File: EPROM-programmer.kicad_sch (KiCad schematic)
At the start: 2 parts, among them U1 ATmega1284-P, U2 MCP2221AxP

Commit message: Some initial stuff
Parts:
- added C1, C2: 22p, Capacitor_THT:C_Rect_L4.6mm_W3.0mm_P2.50mm_MKS02_FKP02, symbol Device:C
- added C3: 100n, Capacitor_THT:C_Rect_L4.6mm_W3.0mm_P2.50mm_MKS02_FKP02, symbol Device:C
- added J1: Conn_02x12_Counter_Clockwise, Local:DIP_Socket-24_W11.9_W12.7_W15.24_W17.78_W18.5_3M_224-1275-00-0602J, symbol Connector_Generic:Conn_02x12_Counter_Clockwise
- added P1: USB_C_Plug_USB2.0, Connector_USB:USB_C_Receptacle_GCT_USB4085, symbol Connector:USB_C_Receptacle_USB2.0
- added R1, R2, R3: 5K1, Resistor_THT:R_Axial_DIN0207_L6.3mm_D2.5mm_P10.16mm_Horizontal, symbol Device:R
- added R4, R5: 470, Resistor_THT:R_Axial_DIN0207_L6.3mm_D2.5mm_P10.16mm_Horizontal, symbol Device:R
- added SW1: SW_Push, symbol Switch:SW_Push
- added Y1: 20M, Crystal:Crystal_HC49-U_Vertical, symbol Device:Crystal
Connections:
- net +5V: now reaches U2.1 (VDD)
- net +5V: now also U1.10 (VCC), U1.30 (AVCC), U1.32 (AREF), P1.A4 (VBUS), P1.A9 (VBUS), P1.B4 (VBUS), P1.B9 (VBUS), R3.1
- net at U2.11 (VUSB): now also C3.1
- net at U2.12 (D-): now also P1.A7 (D-), P1.B7 (D-)
- net at U2.13 (D+): now also P1.A6 (D+), P1.B6 (D+)
- net GND: now reaches U2.14 (VSS)
- net GND: now also U1.11 (GND), U1.31 (GND), C1.2, C2.2, C3.2, P1.A1 (GND), P1.A12 (GND), P1.B1 (GND), P1.B12 (GND), P1.S1 (SHIELD), R1.2, R2.2, SW1.1
- net at U2.2 (GP0): now also R4.2
- net at U2.3 (GP1): now also R5.2
- net TXD: now reaches U2.5 (URx)
- net TXD: now also U1.15 (PD1)
- net RXD: now reaches U2.6 (UTx)
- net RXD: now also U1.14 (PD0)
- net at U1.12 (XTAL2): now also C2.1, Y1.2
- net at U1.13 (XTAL1): now also C1.1, Y1.1
- net at U1.9 (~{RESET}): now also R3.2, SW1.2
- new net: P1.A5 (CC1), R2.1
- new net: P1.B5 (CC2), R1.1
- no-connect marks 0 -> 7
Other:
- moved on the sheet: U1, U2

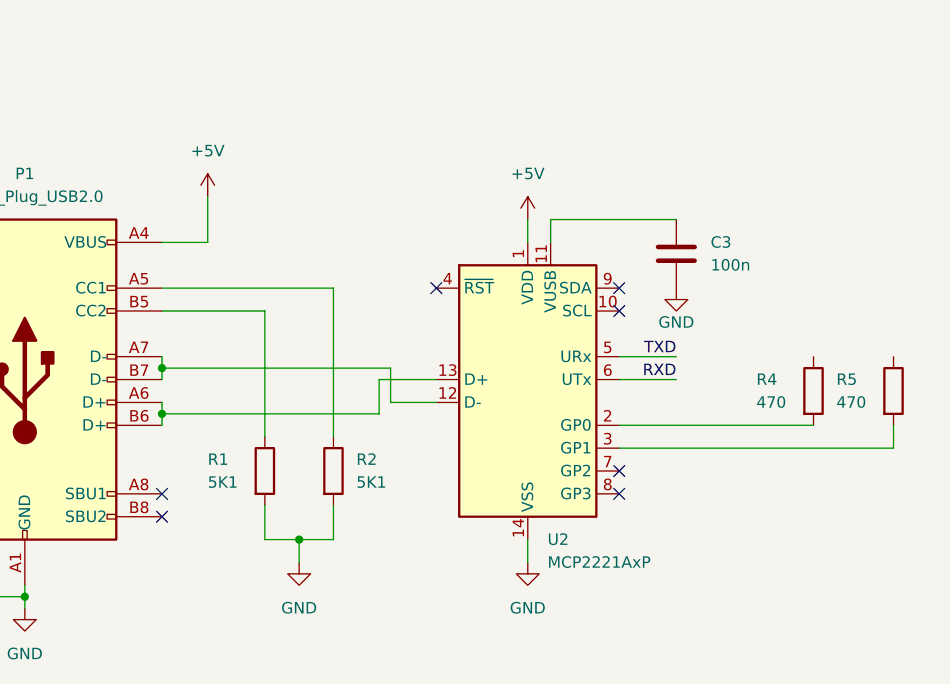
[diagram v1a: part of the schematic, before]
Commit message: Add some LEDs
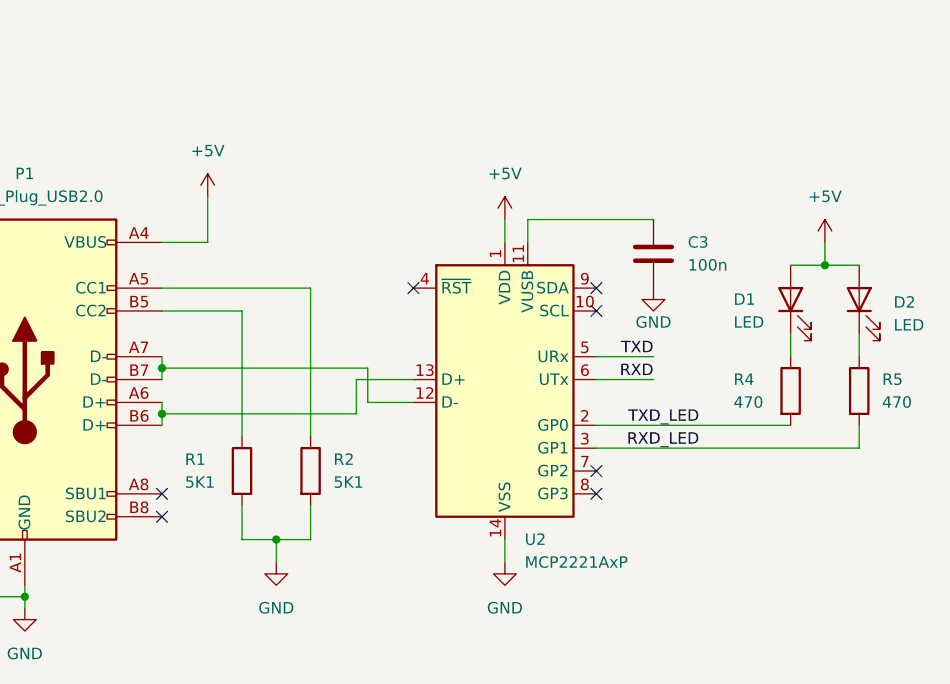
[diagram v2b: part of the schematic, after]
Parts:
- added D1, D2: LED, symbol Device:LED
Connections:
- net +5V: now also D1.2 (A), D2.2 (A)
- net at R4.1: now also D1.1 (K)
- net TXD_LED: now reaches R4.2, U2.2 (GP0)
- net RXD_LED: now reaches R5.2, U2.3 (GP1)
- net at R5.1: now also D2.1 (K)
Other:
- moved on the sheet: C3, R1, R2, R4, R5, U2

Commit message: Add TODO
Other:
- note added: "TODO: Decoupling+Bulk capacitors ISP-header Power + USB-ready LED? Wire ZIF-socket"
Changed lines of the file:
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@@
     (stroke (width 0) (type default))
+  )
+  (text "TODO:\nDecoupling+Bulk capacitors\nISP-header\nPower + USB-ready LED?\nWire ZIF-socket"
+    (at 113.03 40.64 0)
+    (effects (font (size 2.54 2.54)) (justify left bottom))
   )
   (label "RXD" (at 78.74 118.11 180) (fields_autoplaced)

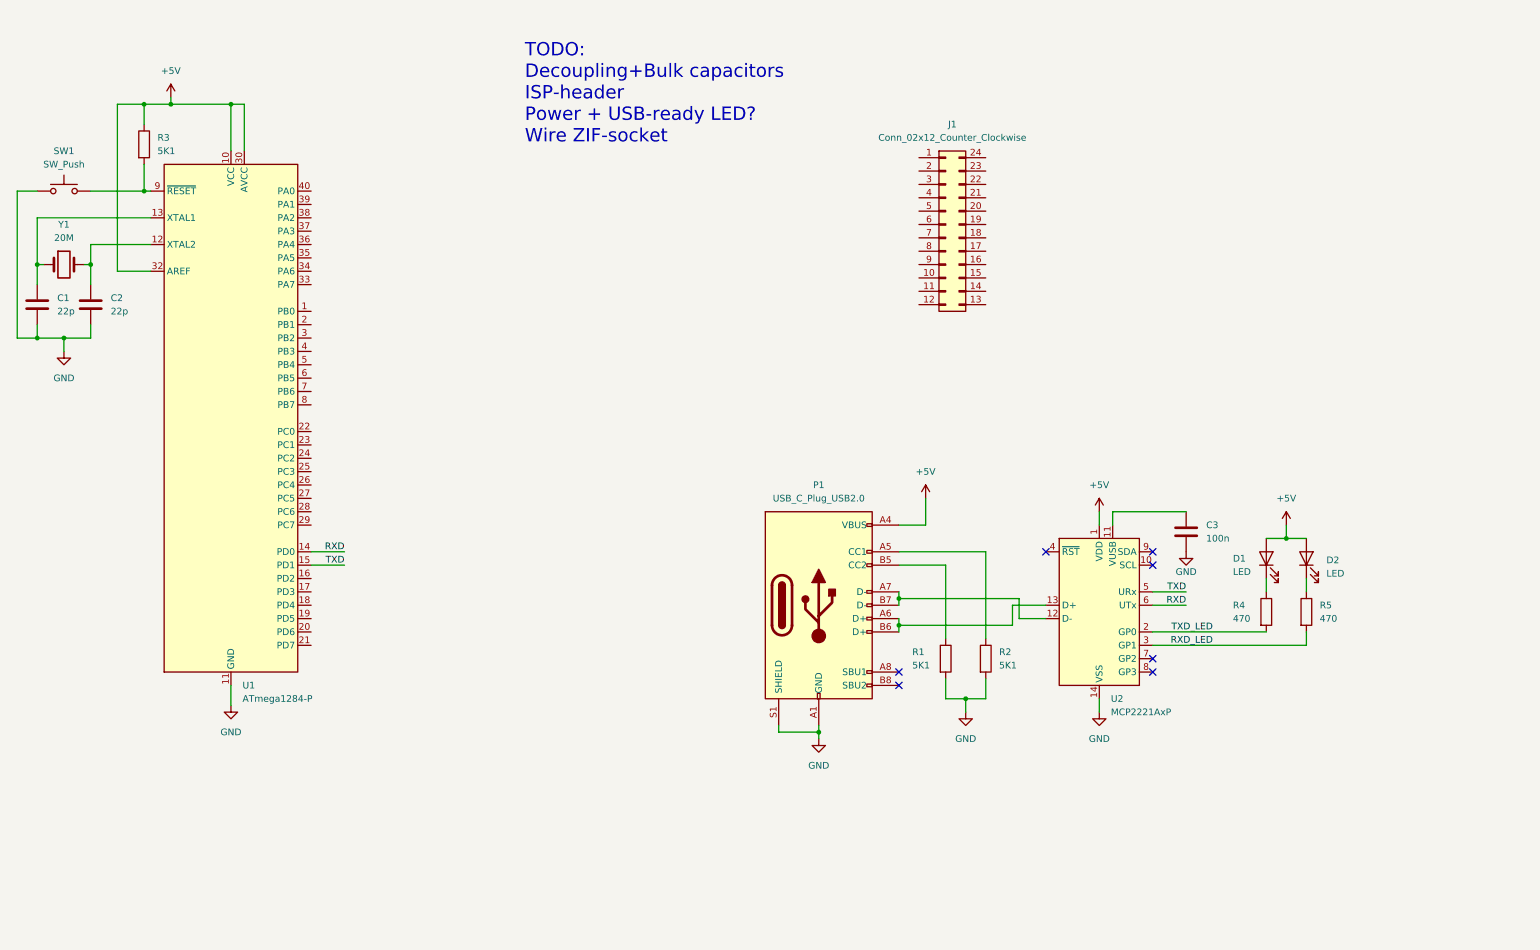
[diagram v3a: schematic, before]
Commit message: Wire-up ISP, ZIF and more
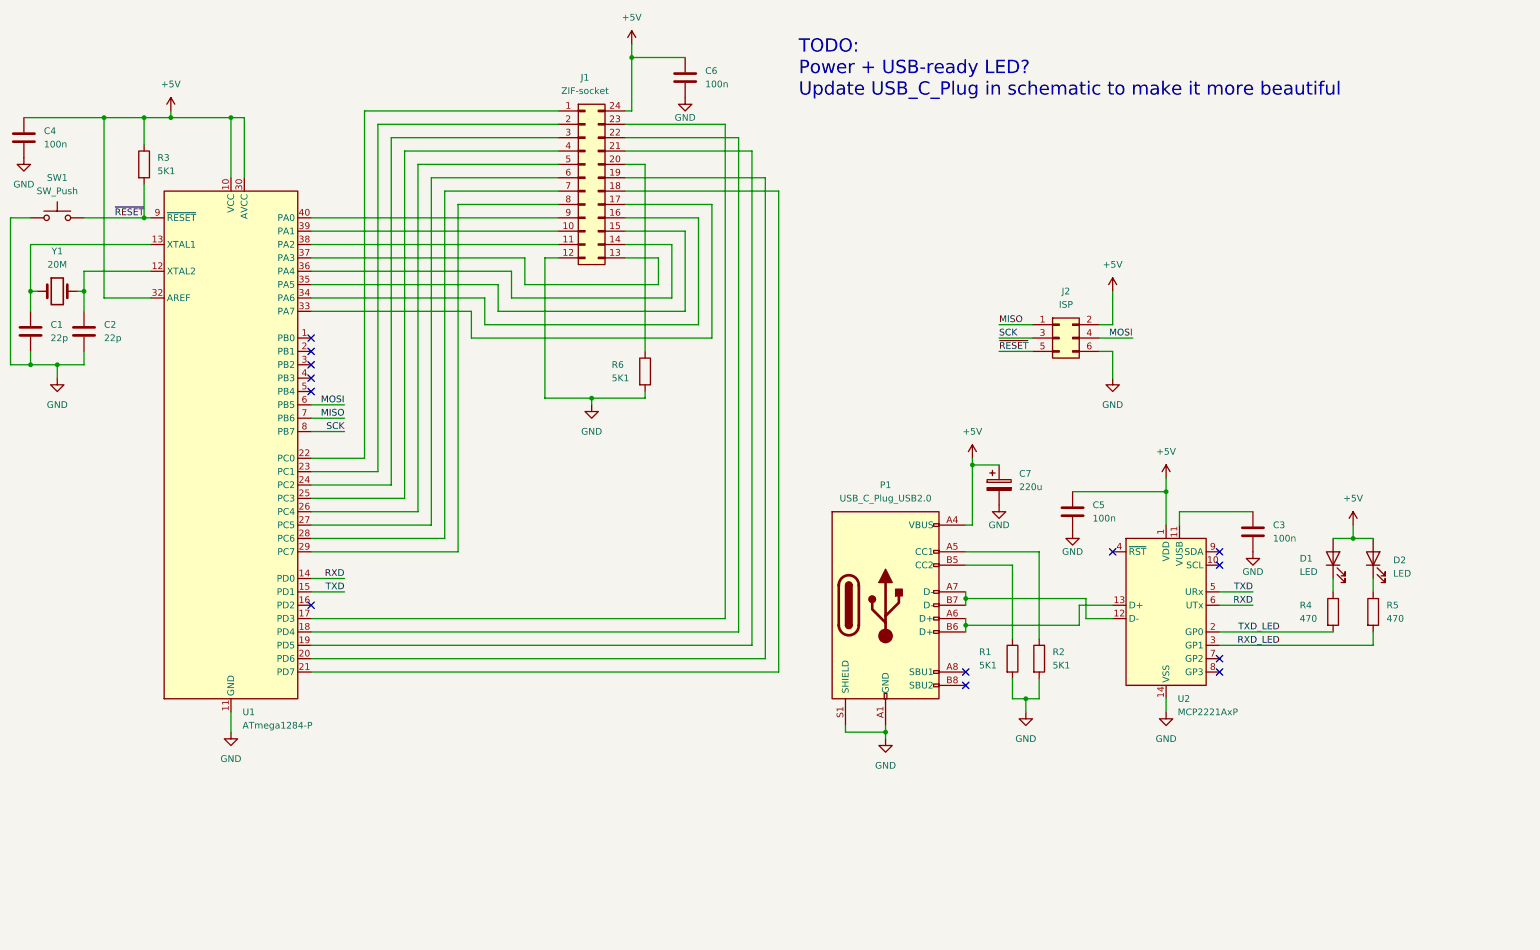
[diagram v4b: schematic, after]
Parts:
- added C4, C5, C6: 100n, Capacitor_THT:C_Rect_L4.6mm_W3.0mm_P2.50mm_MKS02_FKP02, symbol Device:C
- added C7: 220u, symbol Device:C_Polarized
- added J2: ISP, Connector_IDC:IDC-Header_2x03_P2.54mm_Vertical, symbol Connector_Generic:Conn_02x03_Odd_Even
- added R6: 5K1, Resistor_THT:R_Axial_DIN0207_L6.3mm_D2.5mm_P10.16mm_Horizontal, symbol Device:R
- J1: value Conn_02x12_Counter_Clockwise -> ZIF-socket
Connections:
- net +5V: now also J1.24 (Pin_24), C4.1, C5.1, C6.1, C7.1, J2.2 (Pin_2)
- net GND: now also J1.12 (Pin_12), C4.2, C5.2, C6.2, C7.2, J2.6 (Pin_6), R6.2
- net at J1.1 (Pin_1): now also U1.22 (PC0)
- net at J1.10 (Pin_10): now also U1.39 (PA1)
- net at J1.11 (Pin_11): now also U1.38 (PA2)
- net at J1.13 (Pin_13): now also U1.37 (PA3)
- net at J1.14 (Pin_14): now also U1.36 (PA4)
- net at J1.15 (Pin_15): now also U1.35 (PA5)
- net at J1.16 (Pin_16): now also U1.34 (PA6)
- net at J1.17 (Pin_17): now also U1.33 (PA7)
- net at J1.18 (Pin_18): now also U1.21 (PD7)
- net at J1.19 (Pin_19): now also U1.20 (PD6)
- net at J1.2 (Pin_2): now also U1.23 (PC1)
- net at J1.20 (Pin_20): now also R6.1
- net at J1.21 (Pin_21): now also U1.19 (PD5)
- net at J1.22 (Pin_22): now also U1.18 (PD4)
- net at J1.23 (Pin_23): now also U1.17 (PD3)
- net at J1.3 (Pin_3): now also U1.24 (PC2)
- net at J1.4 (Pin_4): now also U1.25 (PC3)
- net at J1.5 (Pin_5): now also U1.26 (PC4)
- net at J1.6 (Pin_6): now also U1.27 (PC5)
- net at J1.7 (Pin_7): now also U1.28 (PC6)
- net at J1.8 (Pin_8): now also U1.29 (PC7)
- net at J1.9 (Pin_9): now also U1.40 (PA0)
- net ~{RESET}: now reaches R3.2, SW1.2, U1.9 (~{RESET})
- net ~{RESET}: now also J2.5 (Pin_5)
- net MOSI: now reaches U1.6 (PB5)
- net MOSI: now also J2.4 (Pin_4)
- net MISO: now reaches U1.7 (PB6)
- net MISO: now also J2.1 (Pin_1)
- net SCK: now reaches U1.8 (PB7)
- net SCK: now also J2.3 (Pin_3)
- no-connect marks 7 -> 13
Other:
- note added: "TODO: Power + USB-ready LED? Update USB_C_Plug in schematic to make it more beautiful"
- note removed: "TODO: Decoupling+Bulk capacitors ISP-header Power + USB-ready LED? Wire ZIF-socket"
- moved on the sheet: C1, C2, C3, D1, D2, J1, P1, R1, R2, R3, R4, R5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

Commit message: Add missing foot-prints
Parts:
- C7: footprint (none) -> Capacitor_THT:CP_Radial_D6.3mm_P2.50mm
- D1, D2: footprint (none) -> LED_THT:LED_D3.0mm
- SW1: footprint (none) -> Button_Switch_THT:SW_PUSH_6mm
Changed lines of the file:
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@@
       (effects (font (size 1.27 1.27)) (justify right))
     )
-    (property "Footprint" "" (at 274.32 119.38 0)
+    (property "Footprint" "LED_THT:LED_D3.0mm" (at 274.32 119.38 0)
       (effects (font (size 1.27 1.27)) hide)
     )
@@
       (effects (font (size 1.27 1.27)))
     )
-    (property "Footprint" "" (at 24.13 49.53 0)
+    (property "Footprint" "Button_Switch_THT:SW_PUSH_6mm" (at 24.13 49.53 0)
       (effects (font (size 1.27 1.27)) hide)
     )
@@
       (effects (font (size 1.27 1.27)) (justify left))
     )
-    (property "Footprint" "" (at 204.1652 109.22 0)
+    (property "Footprint" "Capacitor_THT:CP_Radial_D6.3mm_P2.50mm" (at 204.1652 109.22 0)
       (effects (font (size 1.27 1.27)) hide)
     )
@@
       (effects (font (size 1.27 1.27)) (justify right))
     )
-    (property "Footprint" "" (at 266.7 119.38 0)
-      (effects (font (size 1.27 1.27)) hide)
-    )
+    (property "Footprint" "LED_THT:LED_D3.0mm" (at 266.7 119.38 0)
+      (effects (font (size 1.27 1.27)) hide)
+    )

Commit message: Add power-flags
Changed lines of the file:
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@@
+    (stroke (width 0) (type default))
+  )
+  (wire (pts (xy 252.73 49.53) (xy 252.73 52.07))
     (stroke (width 0) (type default))
   )
@@
   )
   (wire (pts (xy 196.85 125.73) (xy 196.85 127))
+    (stroke (width 0) (type default))
+  )
+  (wire (pts (xy 264.16 52.07) (xy 264.16 49.53))
     (stroke (width 0) (type default))
   )
@@
     )
   )
+  (symbol (lib_id "power:PWR_FLAG") (at 252.73 52.07 180) (unit 1)
+    (in_bom yes) (on_board yes) (dnp no) (fields_autoplaced)
+    (property "Reference" "#FLG01" (at 252.73 53.975 0)
+      (effects (font (size 1.27 1.27)) hide)
+    )
+    (property "Value" "PWR_FLAG" (at 252.73 57.15 0)
+      (effects (font (size 1.27 1.27)))
+    )
+    (property "Footprint" "" (at 252.73 52.07 0)
+      (effects (font (size 1.27 1.27)) hide)
+    )
+    (property "Datasheet" "~" (at 252.73 52.07 0)
+      (effects (font (size 1.27 1.27)) hide)
+    )
+    (pin "1")
+    (instances
+      (project "EPROM-programmer"
+        (path "/8c5576b1-cb3e-4456-837b-2f47818a03ab"
+          (reference "#FLG01") (unit 1)
+        )
+      )
+      (project "MD-Cartridge"
+        (path "/f0e5c94a-c757-4aaf-8df3-cb0b03016f9b"
+          (reference "#FLG01") (unit 1)
+        )
+      )
+    )
+  )
   (symbol (lib_id "Device:R") (at 210.82 138.43 0) (unit 1)
     (in_bom yes) (on_board yes) (dnp no) (fields_autoplaced)
@@
         (path "/8c5576b1-cb3e-4456-837b-2f47818a03ab"
           (reference "SW1") (unit 1)
+        )
+      )
+    )
+  )
+  (symbol (lib_id "power:PWR_FLAG") (at 264.16 49.53 0) (unit 1)
+    (in_bom yes) (on_board yes) (dnp no) (fields_autoplaced)
+    (property "Reference" "#FLG02" (at 264.16 47.625 0)
+      (effects (font (size 1.27 1.27)) hide)
+    )
+    (property "Value" "PWR_FLAG" (at 264.16 45.72 0)
+      (effects (font (size 1.27 1.27)))
+    )
+    (property "Footprint" "" (at 264.16 49.53 0)
+      (effects (font (size 1.27 1.27)) hide)
+    )
+    (property "Datasheet" "~" (at 264.16 49.53 0)
+      (effects (font (size 1.27 1.27)) hide)
+    )
+    (pin "1")
+    (instances
+      (project "EPROM-programmer"
+        (path "/8c5576b1-cb3e-4456-837b-2f47818a03ab"
+          (reference "#FLG02") (unit 1)
+        )
+      )
+      (project "MD-Cartridge"
+        (path "/f0e5c94a-c757-4aaf-8df3-cb0b03016f9b"
+          (reference "#FLG02") (unit 1)
         )
       )
@@
     )
   )
+  (symbol (lib_id "power:+5V") (at 252.73 49.53 0) (unit 1)
+    (in_bom yes) (on_board yes) (dnp no) (fields_autoplaced)
+    (property "Reference" "#PWR019" (at 252.73 53.34 0)
+      (effects (font (size 1.27 1.27)) hide)
+    )
+    (property "Value" "+5V" (at 252.73 45.72 0)
+      (effects (font (size 1.27 1.27)))
+    )
+    (property "Footprint" "" (at 252.73 49.53 0)
+      (effects (font (size 1.27 1.27)) hide)
+    )
+    (property "Datasheet" "" (at 252.73 49.53 0)
+      (effects (font (size 1.27 1.27)) hide)
+    )
+    (pin "1")
+    (instances
+      (project "EPROM-programmer"
+        (path "/8c5576b1-cb3e-4456-837b-2f47818a03ab"
+          (reference "#PWR019") (unit 1)
+        )
+      )
+      (project "MD-Cartridge"
+        (path "/f0e5c94a-c757-4aaf-8df3-cb0b03016f9b"
+          (reference "#PWR08") (unit 1)
+        )
+      )
+    )
+  )
   (symbol (lib_id "Device:R") (at 135.89 83.82 0) (unit 1)
     (in_bom yes) (on_board yes) (dnp no)
@@
         )
       )
+    )
+  )
+  (symbol (lib_id "power:GND") (at 264.16 52.07 0) (unit 1)
+    (in_bom yes) (on_board yes) (dnp no) (fields_autoplaced)
+    (property "Reference" "#PWR020" (at 264.16 58.42 0)
+      (effects (font (size 1.27 1.27)) hide)
+    )
+    (property "Value" "GND" (at 264.16 57.15 0)
+      (effects (font (size 1.27 1.27)))
+    )
+    (property "Footprint" "" (at 264.16 52.07 0)
+      (effects (font (size 1.27 1.27)) hide)
+    )
+    (property "Datasheet" "" (at 264.16 52.07 0)
+      (effects (font (size 1.27 1.27)) hide)
+    )
+    (pin "1")
+    (instances
+      (project "EPROM-programmer"
+        (path "/8c5576b1-cb3e-4456-837b-2f47818a03ab"
+          (reference "#PWR020") (unit 1)
+        )
+      )
+      (project "MD-Cartridge"
+        (path "/f0e5c94a-c757-4aaf-8df3-cb0b03016f9b"
+          (reference "#PWR09") (unit 1)
+        )
+      )

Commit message: Clean-up
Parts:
- added D3: GREEN, LED_THT:LED_D3.0mm, symbol Device:LED
- added R7: 470, Resistor_THT:R_Axial_DIN0207_L6.3mm_D2.5mm_P10.16mm_Horizontal, symbol Device:R
- D1, D2: value LED -> YELLOW
- P1: value USB_C_Plug_USB2.0 -> USB-C; symbol Connector:USB_C_Receptacle_USB2.0 -> EPROM-programmer:USB_C_Receptacle_USB2.0_modified
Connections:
- net +5V: now also D3.2 (A)
- net GND: now also R7.2
- new net: D3.1 (K), R7.1
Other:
- note added: "TODO: USB-ready LED?"
- note removed: "TODO: Power + USB-ready LED? Update USB_C_Plug in schematic to make it more beautiful"
- moved on the sheet: C3, C5, C7, D1, D2, P1, R1, R2, R4, R5, U2
